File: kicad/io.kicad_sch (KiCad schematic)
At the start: 17 parts, among them J10 IO6, J12 LED stick, J5 IO1, J6 IO2, J7 IO3, J8 IO4, J9 IO5, U14 74AHCT1G125

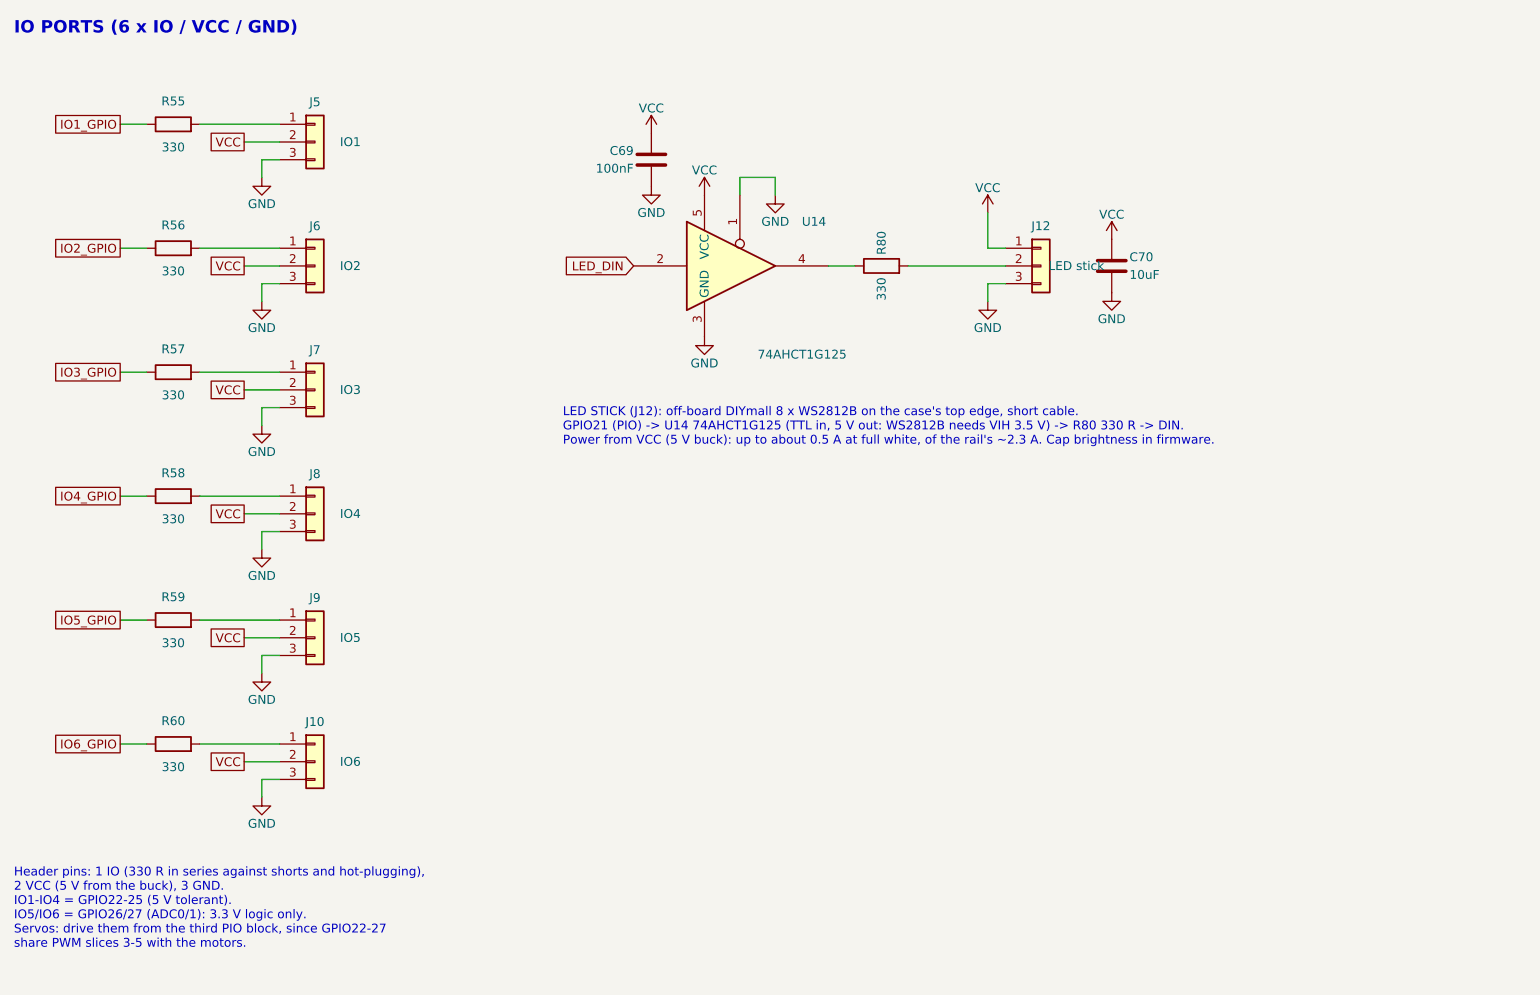
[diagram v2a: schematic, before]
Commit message: Re-lay out rev 2 around an Ovonic 450 pack on top of the board
The internal pack is now an Ovonic 3S 450 mAh XT30 pack sitting 2 mm
above the board over the low-power logic area, on an XT30 pigtail. The
board is 88.5 x 47 mm with 2 mm corner radii, for a box of about
93.5 x 52 x 24.6 mm whose face has no openings.

- IO S1-S6 are a 3 x 6 right-angle header out of the left end, beside
  M5/M6, replacing the recessed vertical block.
- BOOT is a side-push switch on the top edge behind a pinhole sized for
  a 2.5 mm hex key; RESET is removed, with RUN on a bottom test pad
  beside SWCLK/SWDIO/GND.
- The CHG LED is a side-view part on the top edge; the GPIO status LED
  is removed now that the WS2812B stick shows status.
- The pack NTC is removed (a fixed 10k holds the charger's TS at 25 C);
  the protector's on-board TH1 stays.
- Q1, F1 and the other warm parts moved out from under the pack, and the
  GPIO map was re-swapped for the new placement (I2C on I2C1).

Schematic review passes; PCB review passes every gate except unrouted.

Co-Authored-By: Claude Opus 5.5 <noreply@anthropic.com>
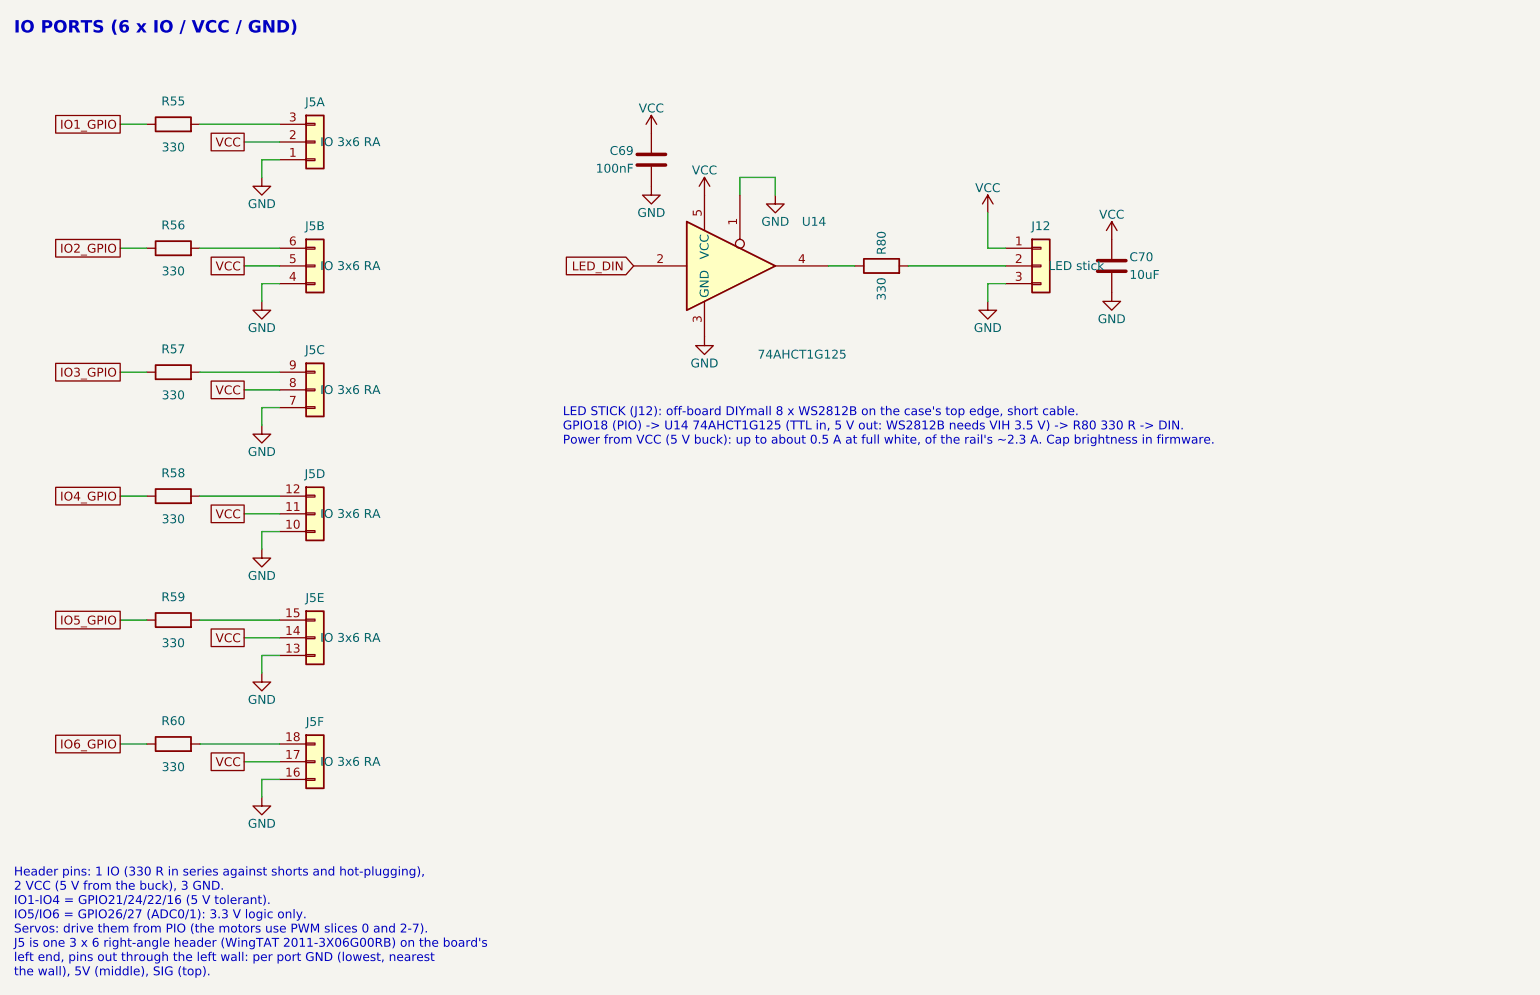
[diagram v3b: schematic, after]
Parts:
- J5: renamed from J8; value IO4 -> IO 3x6 RA; footprint Connector_PinHeader_2.54mm:PinHeader_1x03_P2.54mm_Vertical -> hexy:PinHeader_3x06_P2.54mm_Horizontal_WingTAT; symbol Connector_Generic:Conn_01x03 -> hexyhustle:IO_3x6_RA; LCSC Part # C49257 -> C51953246; MPN 2.54-1*3P -> 2011-3X06G00RB; Manufacturer BOOMELE(Boom Precision Elec) -> WingTAT
- J5: renamed from J7; value IO3 -> IO 3x6 RA; footprint Connector_PinHeader_2.54mm:PinHeader_1x03_P2.54mm_Vertical -> hexy:PinHeader_3x06_P2.54mm_Horizontal_WingTAT; symbol Connector_Generic:Conn_01x03 -> hexyhustle:IO_3x6_RA; LCSC Part # C49257 -> C51953246; MPN 2.54-1*3P -> 2011-3X06G00RB; Manufacturer BOOMELE(Boom Precision Elec) -> WingTAT
- J5: renamed from J9; value IO5 -> IO 3x6 RA; footprint Connector_PinHeader_2.54mm:PinHeader_1x03_P2.54mm_Vertical -> hexy:PinHeader_3x06_P2.54mm_Horizontal_WingTAT; symbol Connector_Generic:Conn_01x03 -> hexyhustle:IO_3x6_RA; LCSC Part # C49257 -> C51953246; MPN 2.54-1*3P -> 2011-3X06G00RB; Manufacturer BOOMELE(Boom Precision Elec) -> WingTAT
- J5: renamed from J6; value IO2 -> IO 3x6 RA; footprint Connector_PinHeader_2.54mm:PinHeader_1x03_P2.54mm_Vertical -> hexy:PinHeader_3x06_P2.54mm_Horizontal_WingTAT; symbol Connector_Generic:Conn_01x03 -> hexyhustle:IO_3x6_RA; LCSC Part # C49257 -> C51953246; MPN 2.54-1*3P -> 2011-3X06G00RB; Manufacturer BOOMELE(Boom Precision Elec) -> WingTAT
- J5: renamed from J10; value IO6 -> IO 3x6 RA; footprint Connector_PinHeader_2.54mm:PinHeader_1x03_P2.54mm_Vertical -> hexy:PinHeader_3x06_P2.54mm_Horizontal_WingTAT; symbol Connector_Generic:Conn_01x03 -> hexyhustle:IO_3x6_RA; LCSC Part # C49257 -> C51953246; MPN 2.54-1*3P -> 2011-3X06G00RB; Manufacturer BOOMELE(Boom Precision Elec) -> WingTAT
- J5: value IO1 -> IO 3x6 RA; footprint Connector_PinHeader_2.54mm:PinHeader_1x03_P2.54mm_Vertical -> hexy:PinHeader_3x06_P2.54mm_Horizontal_WingTAT; symbol Connector_Generic:Conn_01x03 -> hexyhustle:IO_3x6_RA; LCSC Part # C49257 -> C51953246; MPN 2.54-1*3P -> 2011-3X06G00RB; Manufacturer BOOMELE(Boom Precision Elec) -> WingTAT
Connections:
- net GND: now also J5.1 (GND), J5.10 (GND), J5.13 (GND), J5.16 (GND), J5.4 (GND), J5.7 (GND); no longer J5.3 (Pin_3), J5.3 (Pin_3), J5.3 (Pin_3), J5.3 (Pin_3), J5.3 (Pin_3), J5.3 (Pin_3)
- net VCC: now also J5.11 (5V), J5.14 (5V), J5.17 (5V), J5.5 (5V), J5.8 (5V); no longer J5.2 (Pin_2), J5.2 (Pin_2), J5.2 (Pin_2), J5.2 (Pin_2), J5.2 (Pin_2)
- net at R56.2: now also J5.6 (SIG); no longer J5.1 (Pin_1)
- net at R58.2: now also J5.12 (SIG); no longer J5.1 (Pin_1)
- net at R57.2: now also J5.9 (SIG); no longer J5.1 (Pin_1)
- net at R60.2: now also J5.18 (SIG); no longer J5.1 (Pin_1)
- net at R59.2: now also J5.15 (SIG); no longer J5.1 (Pin_1)
- net at R55.2: now also J5.3 (SIG); no longer J5.1 (Pin_1)
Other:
- note added: "Header pins: 1 IO (330 R in series against shorts and hot-plugging), 2 VCC (5 V from the buck), 3 GND. IO1-IO4 = GPIO21/24/22/16 (5 V tolerant). IO5/IO6 = GPIO26/27 (ADC0/1): 3.3 V logic only. Servos: drive them from PIO (the motors use PWM slices 0 and 2-7). J5 is one 3 x 6 right-angle header (WingTAT 2011-3X06G00RB) on the board's left end, pins out through the left wall: per port GND (lowest, 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"
- note added: "LED STICK (J12): off-board DIYmall 8 x WS2812B on the case's top edge, short cable. GPIO18 (PIO) -> U14 74AHCT1G125 (TTL in, 5 V out: WS2812B needs VIH 3.5 V) -> R80 330 R -> DIN. Power from VCC (5 V buck): up to about 0.5 A at full white, of the rail's ~2.3 A. Cap brightness in firmware."
- note removed: "Header pins: 1 IO (330 R in series against shorts and hot-plugging), 2 VCC (5 V from the buck), 3 GND. IO1-IO4 = GPIO22-25 (5 V tolerant). IO5/IO6 = GPIO26/27 (ADC0/1): 3.3 V logic only. Servos: drive them from the third PIO block, since GPIO22-27 share PWM slices 3-5 with the motors."
- note removed: "LED STICK (J12): off-board DIYmall 8 x WS2812B on the case's top edge, short cable. GPIO21 (PIO) -> U14 74AHCT1G125 (TTL in, 5 V out: WS2812B needs VIH 3.5 V) -> R80 330 R -> DIN. Power from VCC (5 V buck): up to about 0.5 A at full white, of the rail's ~2.3 A. Cap brightness in firmware."

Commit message: Fit the standard Ovonic 450 pack and recess the IO header
The earlier 50.5 x 25 x 14 mm pack size came from a mislabeled listing.
The layout now uses the standard Ovonic 80C 3S 450 mAh pack (design
envelope 46.5 x 25 x 21 mm) on top of the board, for a box of about
93.5 x 52 x 30 mm; the Long Size pack would have needed a ~110 mm box.

- S1-S6 (J5) move 5.55 mm inboard so the pin tips end 1 mm inside the
  left wall; the FET/shunt strip and nearby passives shift to suit.
- The pack carries a female XT30U-F, so J3 takes a male XT30U-M pigtail
  on 16 AWG. A vertical XT30UPB-M was checked and misses the 1 mm
  clearance under the face.
- IO1-IO4 GPIOs reordered for the new placement.

Schematic review passes; PCB review passes every gate except unrouted.

Co-Authored-By: Claude Opus 5.5 <noreply@anthropic.com>
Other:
- note added: "Header pins: 1 IO (330 R in series against shorts and hot-plugging), 2 VCC (5 V from the buck), 3 GND. IO1-IO4 = GPIO16/21/22/24 (5 V tolerant). IO5/IO6 = GPIO26/27 (ADC0/1): 3.3 V logic only. Servos: drive them from PIO (the motors use PWM slices 0 and 2-7). J5 is one 3 x 6 right-angle header (WingTAT 2011-3X06G00RB) on the board's left end, pins out through the left wall: per port GND (lowest, 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"
- note removed: "Header pins: 1 IO (330 R in series against shorts and hot-plugging), 2 VCC (5 V from the buck), 3 GND. IO1-IO4 = GPIO21/24/22/16 (5 V tolerant). IO5/IO6 = GPIO26/27 (ADC0/1): 3.3 V logic only. Servos: drive them from PIO (the motors use PWM slices 0 and 2-7). J5 is one 3 x 6 right-angle header (WingTAT 2011-3X06G00RB) on the board's left end, pins out through the left wall: per port GND (lowest, 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"
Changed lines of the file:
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@@
 		)
 	)
-	(text "Header pins: 1 IO (330 R in series against shorts and hot-plugging),\n2 VCC (5 V from the buck), 3 GND.\nIO1-IO4 = GPIO21/24/22/16 (5 V tolerant).\nIO5/IO6 = GPIO26/27 (ADC0/1): 3.3 V logic only.\nServos: drive them from PIO (the motors use PWM slices 0 and 2-7).\nJ5 is one 3 x 6 right-angle header (WingTAT 2011-3X06G00RB) on the board's\nleft end, pins out through the left wall: per port GND (lowest, nearest\nthe wall), 5V (middle), SIG (top)."
+	(text "Header pins: 1 IO (330 R in series against shorts and hot-plugging),\n2 VCC (5 V from the buck), 3 GND.\nIO1-IO4 = GPIO16/21/22/24 (5 V tolerant).\nIO5/IO6 = GPIO26/27 (ADC0/1): 3.3 V logic only.\nServos: drive them from PIO (the motors use PWM slices 0 and 2-7).\nJ5 is one 3 x 6 right-angle header (WingTAT 2011-3X06G00RB) on the board's\nleft end, pins out through the left wall: per port GND (lowest, nearest\nthe wall), 5V (middle), SIG (top)."
 		(exclude_from_sim no)
 		(at 86.36 152.4 0)

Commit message: Fix the buck inductor, soft-start VSYS and limit motor current
Circuit (goosebrain.py, PARTS.md, schematic):
- L1 is a Coilcraft XAL5030-222 (Isat 9.2 A, the AP64500's max current
  limit). The old CR4030 saturated at about 3.1 A.
- VSYS soft start and clamp: C71 gate-drain and C72 gate-source on Q1,
  R40 27k, R41 10k, and an SMF14A TVS (D4) on VSYS.
- Each DRV8848 chops at about 1.33 A per bridge: 0.15 R sense resistors
  on AISEN/BISEN and a 15k/10k VREF divider from VINT, so six stalled
  motors can't reach the protector's OCD1 trip.
- U4 gets a second 10 uF (C73) and a 100 nF (C74) at VIN.
- Stock swaps after a full JLC stock check: D4 to the Littelfuse SMF14A,
  the sense resistors to YAGEO RL1206FR-7W0R15L (500 mW).

Board:
- New parts placed and routed. The sense resistors are close to their
  pins; U2's B-side runs on F.Cu only.
- 22 more VSYS vias (Q1 drain to the In3 plane, each driver's VM caps,
  both ends of U4's VIN jumper).
- C63 (AVDD) and C68 (SRP-SRN) moved next to the BQ7791501.
- Goose logo on the back silkscreen.
- Review 63: DRC 0 errors, unrouted 0, parity clean, no new DRC types.

tools/fab.py adds per-package rotation offsets read off JLC's placement
preview. The README covers them, the D4 polarity check, the corrected
current limits and the low-stock parts.

Co-Authored-By: Claude Opus 5.5 <noreply@anthropic.com>
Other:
- note added: "LED STICK (J12): off-board DIYmall 8 x WS2812B on the case's top edge, short cable. GPIO18 (PIO) -> U14 74AHCT1G125 (TTL in, 5 V out: WS2812B needs VIH 3.5 V) -> R80 330 R -> DIN. Power from VCC (5 V buck, shared with the IO ports): up to about 0.5 A at full white. Cap brightness in firmware."
- note added: "Per port: pin 3k SIG (330 R in series against shorts and hot-plugging), 3k-1 VCC (5 V from the buck), 3k-2 GND; e.g. J5A: 3 SIG, 2 VCC, 1 GND. IO1-IO4 = GPIO16/21/22/24 (5 V tolerant). IO5/IO6 = GPIO26/27 (ADC0/1): 3.3 V logic only. Servos: drive them from PIO (the motors use PWM slices 0 and 2-7). J5 is one 3 x 6 right-angle header (WingTAT 2011-3X06G00RB) on the board's left end, pins out throu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"
- note removed: "Header pins: 1 IO (330 R in series against shorts and hot-plugging), 2 VCC (5 V from the buck), 3 GND. IO1-IO4 = GPIO16/21/22/24 (5 V tolerant). IO5/IO6 = GPIO26/27 (ADC0/1): 3.3 V logic only. Servos: drive them from PIO (the motors use PWM slices 0 and 2-7). J5 is one 3 x 6 right-angle header (WingTAT 2011-3X06G00RB) on the board's left end, pins out through the left wall: per port GND (lowest, 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"
- note removed: "LED STICK (J12): off-board DIYmall 8 x WS2812B on the case's top edge, short cable. GPIO18 (PIO) -> U14 74AHCT1G125 (TTL in, 5 V out: WS2812B needs VIH 3.5 V) -> R80 330 R -> DIN. Power from VCC (5 V buck): up to about 0.5 A at full white, of the rail's ~2.3 A. Cap brightness in firmware."
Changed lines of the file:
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@@
 		)
 		(property "Value" "IO 3x6 RA"
-			(at 134.62 48.26 0)
+			(at 139.7 48.26 0)
 			(show_name no)
 			(do_not_autoplace no)
@@
 		)
 		(property "Value" "IO 3x6 RA"
-			(at 134.62 66.04 0)
+			(at 139.7 66.04 0)
 			(show_name no)
 			(do_not_autoplace no)
@@
 		)
 		(property "Value" "IO 3x6 RA"
-			(at 134.62 83.82 0)
+			(at 139.7 83.82 0)
 			(show_name no)
 			(do_not_autoplace no)
@@
 		)
 		(property "Value" "IO 3x6 RA"
-			(at 134.62 101.60 0)
+			(at 139.7 101.60 0)
 			(show_name no)
 			(do_not_autoplace no)
@@
 		)
 		(property "Value" "IO 3x6 RA"
-			(at 134.62 119.38 0)
+			(at 139.7 119.38 0)
 			(show_name no)
 			(do_not_autoplace no)
@@
 		)
 		(property "Value" "IO 3x6 RA"
-			(at 134.62 137.16 0)
+			(at 139.7 137.16 0)
 			(show_name no)
 			(do_not_autoplace no)
@@
 		)
 	)
-	(text "Header pins: 1 IO (330 R in series against shorts and hot-plugging),\n2 VCC (5 V from the buck), 3 GND.\nIO1-IO4 = GPIO16/21/22/24 (5 V tolerant).\nIO5/IO6 = GPIO26/27 (ADC0/1): 3.3 V logic only.\nServos: drive them from PIO (the motors use PWM slices 0 and 2-7).\nJ5 is one 3 x 6 right-angle header (WingTAT 2011-3X06G00RB) on the board's\nleft end, pins out through the left wall: per port GND (lowest, nearest\nthe wall), 5V (middle), SIG (top)."
+	(text "Per port: pin 3k SIG (330 R in series against shorts and hot-plugging),\n3k-1 VCC (5 V from the buck), 3k-2 GND; e.g. J5A: 3 SIG, 2 VCC, 1 GND.\nIO1-IO4 = GPIO16/21/22/24 (5 V tolerant).\nIO5/IO6 = GPIO26/27 (ADC0/1): 3.3 V logic only.\nServos: drive them from PIO (the motors use PWM slices 0 and 2-7).\nJ5 is one 3 x 6 right-angle header (WingTAT 2011-3X06G00RB) on the board's\nleft end, pins out through the left wall: per port GND (lowest, nearest\nthe wall), 5V (middle), SIG (top)."
 		(exclude_from_sim no)
 		(at 86.36 152.4 0)
@@
 		)
 		(property "Value" "LED stick"
-			(at 238.76 66.04 0)
+			(at 233.68 72.39 0)
 			(show_name no)
 			(do_not_autoplace no)
@@
 		)
 	)
-	(text "LED STICK (J12): off-board DIYmall 8 x WS2812B on the case's top edge, short cable.\nGPIO18 (PIO) -> U14 74AHCT1G125 (TTL in, 5 V out: WS2812B needs VIH 3.5 V) -> R80 330 R -> DIN.\nPower from VCC (5 V buck): up to about 0.5 A at full white, of the rail's ~2.3 A. Cap brightness in firmware."
+	(text "LED STICK (J12): off-board DIYmall 8 x WS2812B on the case's top edge, short cable.\nGPIO18 (PIO) -> U14 74AHCT1G125 (TTL in, 5 V out: WS2812B needs VIH 3.5 V) -> R80 330 R -> DIN.\nPower from VCC (5 V buck, shared with the IO ports): up to about 0.5 A at full white. Cap brightness in firmware."
 		(exclude_from_sim no)
 		(at 165.1 86.36 0)

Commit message: Split into brain + smart pack, and support 2S packs
Brain/pack split: charging, protection and the fuse move off the brain
into a separate smart pack board (kicad-pack/goosepack), with its own
USB-C charging port. The brain drops to 4 layers, loses the charger,
PD sink, protector and SY6280, and swaps the DRV8848s for DRV8871s.

2S support on the brain:
- DRV8871 -> DRV8251A (same HSOP-8 footprint, 4.5-48 V VM). Shared VREF
  divider R107/R108/C81 from +3V3 (2.53 V) and 1.18k IPROPI resistors
  keep the 1.36 A limit.
- Q1 gate divider 27k/10k -> 47k/4.7k for -5.1 V drive at an empty 2S
  pack; C71 4.7n -> 10n to keep the ~70 us soft start.

New 2S pack variant (kicad-pack-2s/goosepack2s): BQ25798 PROG 8.2k
(2S, 750 kHz), ILIM R33 18k (~0.42 A charge), ABLIC S-8252AAH protector
in place of the BQ7791501, two HY2213-BB3A balancers with AO3400A and
47R 2512 bleed resistors, 3-pin XH balance header, R94 4.7k for trip
recovery. fab.py builds it with --board pack2s.

Several new parts still need LCSC numbers; fab.py flags each one.

Co-Authored-By: Claude Opus 5.5 <noreply@anthropic.com>
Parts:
- removed C70: 10uF, Capacitor_SMD:C_0805_2012Metric, symbol Device:C
- removed R80: 330, Resistor_SMD:R_0402_1005Metric, symbol Device:R
- U14: now not fitted
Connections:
- net at U14.4: now also J12.2 (Pin_2)
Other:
- note added: "LED STICK (J12): off-board DIYmall 8 x WS2812B on the case's top edge, short cable. GPIO18 (PIO) -> U14 74AHCT1G125 (TTL in, 5 V out: WS2812B needs VIH 3.5 V; hand-placed) -> DIN. R80 (330 R) and C70 (10 uF) were removed in the cost-down; the stick carries its own caps. Power from VCC (5 V buck, shared with the IO ports): up to about 0.5 A at full white. Cap brightness in firmware."
- note removed: "LED STICK (J12): off-board DIYmall 8 x WS2812B on the case's top edge, short cable. GPIO18 (PIO) -> U14 74AHCT1G125 (TTL in, 5 V out: WS2812B needs VIH 3.5 V) -> R80 330 R -> DIN. Power from VCC (5 V buck, shared with the IO ports): up to about 0.5 A at full white. Cap brightness in firmware."
